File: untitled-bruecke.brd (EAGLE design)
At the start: 100 x 80 mm, 7 parts

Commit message: layout OK
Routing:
- net D6: track 122.9 -> 113.9 mm, vias 2 -> 4
- net D5: track 55.0 -> 49.9 mm
- net B2: track 134.5 -> 131.4 mm
- net C6: track 125.6 -> 128.6 mm, vias 8 -> 6
- net D4: track 113.5 -> 110.5 mm
- net B3: track 124.4 -> 127.4 mm
- net B5: track 171.0 -> 168.1 mm
- net D1: track 46.8 -> 49.6 mm
- net C5: track 133.4 -> 135.2 mm, vias 6 -> 5
- net B1: track 125.5 -> 124.0 mm, vias 4 -> 3
- net B0: track 129.8 -> 128.4 mm
- net C4: track 90.1 -> 89.1 mm
- net D0: track 41.3 -> 40.6 mm
- net C0: vias 5 -> 4

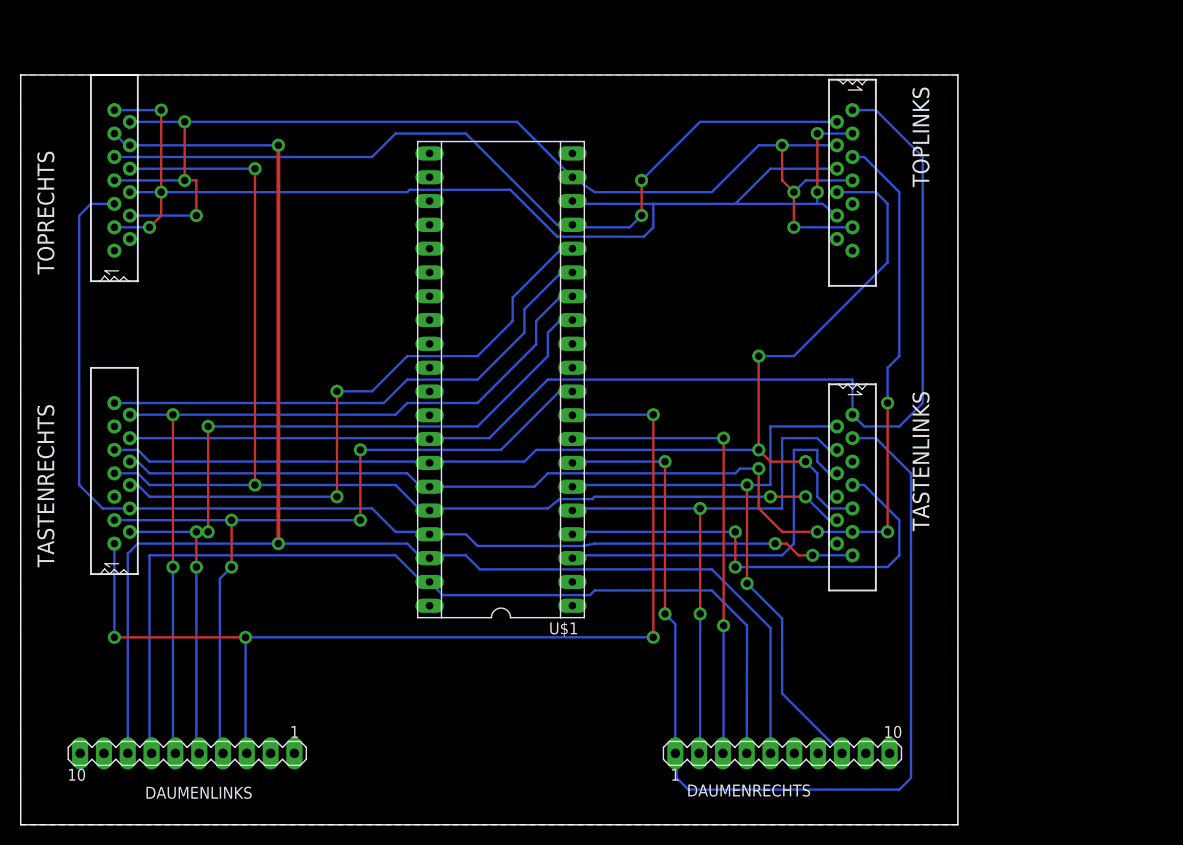
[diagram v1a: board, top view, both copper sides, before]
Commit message: Board für die Fräse vorbereitet
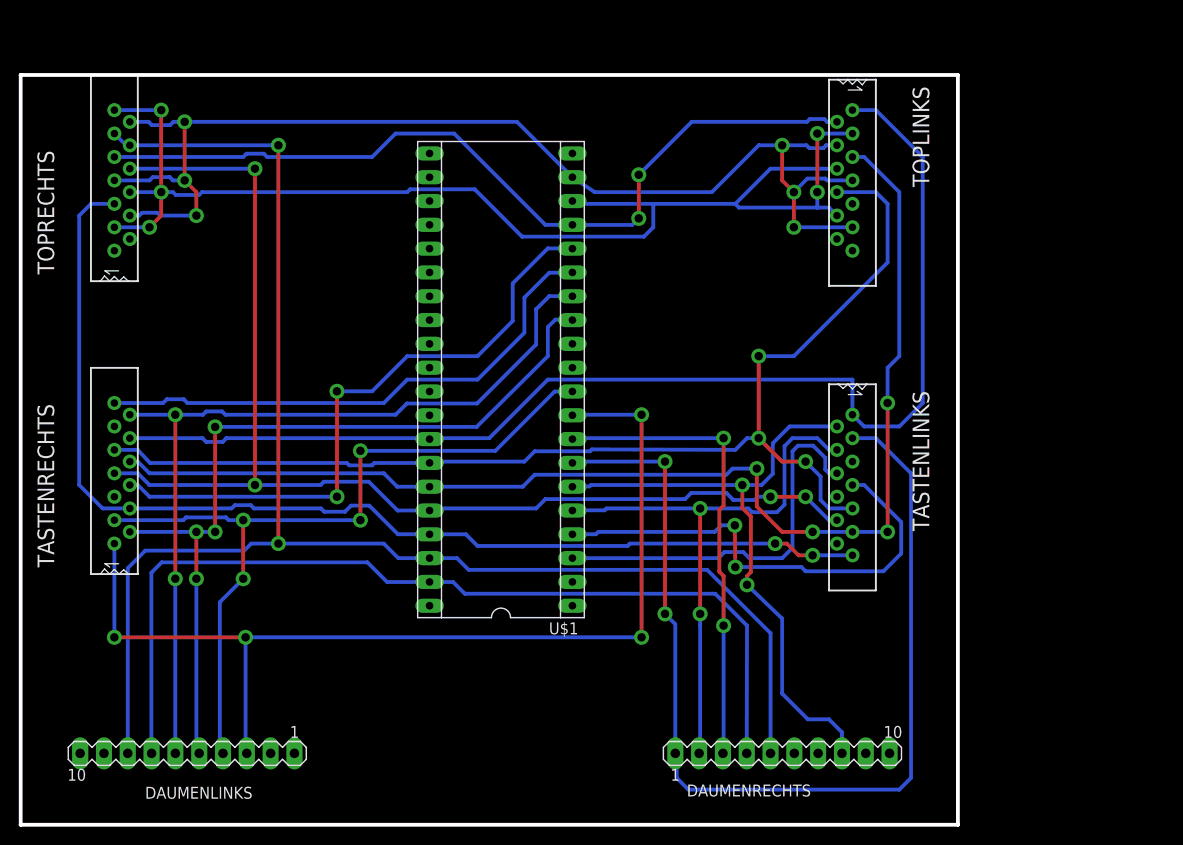
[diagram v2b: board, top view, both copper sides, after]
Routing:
- net D6: track 113.9 -> 111.4 mm
- net B6: track 102.0 -> 99.7 mm
- net D1: track 49.6 -> 51.0 mm
- net B5: track 168.1 -> 166.7 mm
- net D0: track 40.6 -> 41.7 mm
- net C2: track 56.1 -> 57.2 mm
- net B3: track 127.4 -> 128.3 mm
- net C1: track 90.2 -> 91.1 mm
- net B4: track 118.8 -> 119.7 mm
- net C3: track 66.8 -> 67.7 mm
- net C4: track 89.1 -> 90.0 mm
- net C5: track 135.2 -> 135.9 mm
- net D7: track 84.5 -> 85.2 mm
- net D5: track 49.9 -> 50.6 mm
- net C6: track 128.6 -> 129.1 mm

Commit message: Layout fertiggestellt fürs PCB
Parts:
- removed U$1: C-TEENSY++, teensypp:TEENSY++
- added E$1: (no value), holes:3,2-PAD
- added LED1, LED2, LED3, LED4: (no value), led:LED3MM
- added R1, R2, R3, R4: (no value), rcl:R1206
- added U1: C-TEENSY++, teensypp:TEENSY++
- moved TASTENRECHTS 99.2 mm to (108.5, 25.5), flipped to the bottom
- moved TOPRECHTS 95.1 mm to (105.0, 73.5), flipped to the bottom
- moved DAUMENLINKS 81.7 mm to (99.5, 7.00), flipped to the bottom
- moved TASTENLINKS 75.5 mm to (14.0, 25.5), flipped to the bottom
- moved TOPLINKS 71.9 mm to (17.0, 73.5), flipped to the bottom
- moved DAUMENRECHTS 58.8 mm to (22.5, 7.00), flipped to the bottom
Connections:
- removed net VCC: U$1.+5V
- new net N$10: R4.2, U1.F0
- new net N$11: LED1.A, LED2.A, LED3.A, LED4.A, U1.+5V
- new net N$14: LED4.K, R4.1
- new net N$15: LED3.K, R3.1
- new net N$16: LED2.K, R2.1
- new net N$17: LED1.K, R1.1
- new net N$7: R1.2, U1.F3
- new net N$8: R2.2, U1.F2
- new net N$9: R3.2, U1.F1
- net B0: now also U1.B0; no longer U$1.B0
- net B1: now also U1.B1; no longer U$1.B1
- net B2: now also U1.B2; no longer U$1.B2
- net B3: now also TASTENLINKS.P$12, U1.B3; no longer TASTENLINKS.P$10, U$1.B3
- net B4: now also U1.B4; no longer U$1.B4
- net B5: now also U1.B5; no longer U$1.B5
- net B6: now also U1.B6; no longer U$1.B6
- net C0: now also U1.C0; no longer U$1.C0
- net C1: now also U1.C1; no longer U$1.C1
- net C2: now also U1.C2; no longer U$1.C2
- net C3: now also U1.C3; no longer U$1.C3
- net C4: now also U1.C4; no longer U$1.C4
- net C5: now also U1.C5; no longer U$1.C5
- net C6: now also U1.C6; no longer U$1.C6
- net D0: now also TASTENLINKS.P$8, U1.D0; no longer TASTENLINKS.P$6, U$1.D0
- net D1: now also U1.D1; no longer U$1.D1
- net D2: now also TASTENLINKS.P$6, U1.D2; no longer TASTENLINKS.P$4, U$1.D2
- net D3: now also TASTENLINKS.P$4, U1.D3; no longer TASTENLINKS.P$2, U$1.D3
- net D4: now also U1.D4; no longer U$1.D4
- net D5: now also TASTENLINKS.P$2, U1.D5; no longer U$1.D5
- net D6: now also U1.D6; no longer U$1.D6
- net D7: now also U1.D7; no longer U$1.D7
- net GND: now also U1.GRND1; no longer U$1.GRND1
- net N$1: now also U1.GND; no longer U$1.GND
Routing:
- net N$11: track 0.00 -> 72.8 mm
- net D5: track 50.6 -> 122.0 mm, vias 2 -> 0
- net D7: track 85.2 -> 143.6 mm, vias 4 -> 0
- net B4: track 119.7 -> 172.5 mm, vias 2 -> 1
- net D2: track 62.1 -> 109.6 mm, vias 2 -> 0
- net D0: track 41.7 -> 85.3 mm
- net N$10: track 0.00 -> 42.7 mm
- net C0: track 88.7 -> 128.0 mm, vias 4 -> 1
- net B1: track 124.1 -> 162.9 mm, vias 3 -> 1
- net B3: track 128.3 -> 166.9 mm, vias 4 -> 1
- net B2: track 131.2 -> 167.9 mm, vias 4 -> 1
- net N$9: track 0.00 -> 36.0 mm
- net D3: track 67.5 -> 102.2 mm, vias 2 -> 0
- net D6: track 111.4 -> 144.6 mm, vias 4 -> 0
- net D1: track 51.0 -> 83.3 mm, vias 2 -> 0
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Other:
- board size 100 x 80 mm -> 122 x 86 mm
- board text added: "28.02.2013"
- board text added: "CAPS"
- board text added: "KEYPAD"
- board text added: "M. Stapelberg / V. Wunsch"
- board text added: "NUM"
- board text added: "SCR"
- board text added: "Teensy++ Kinesis controller"

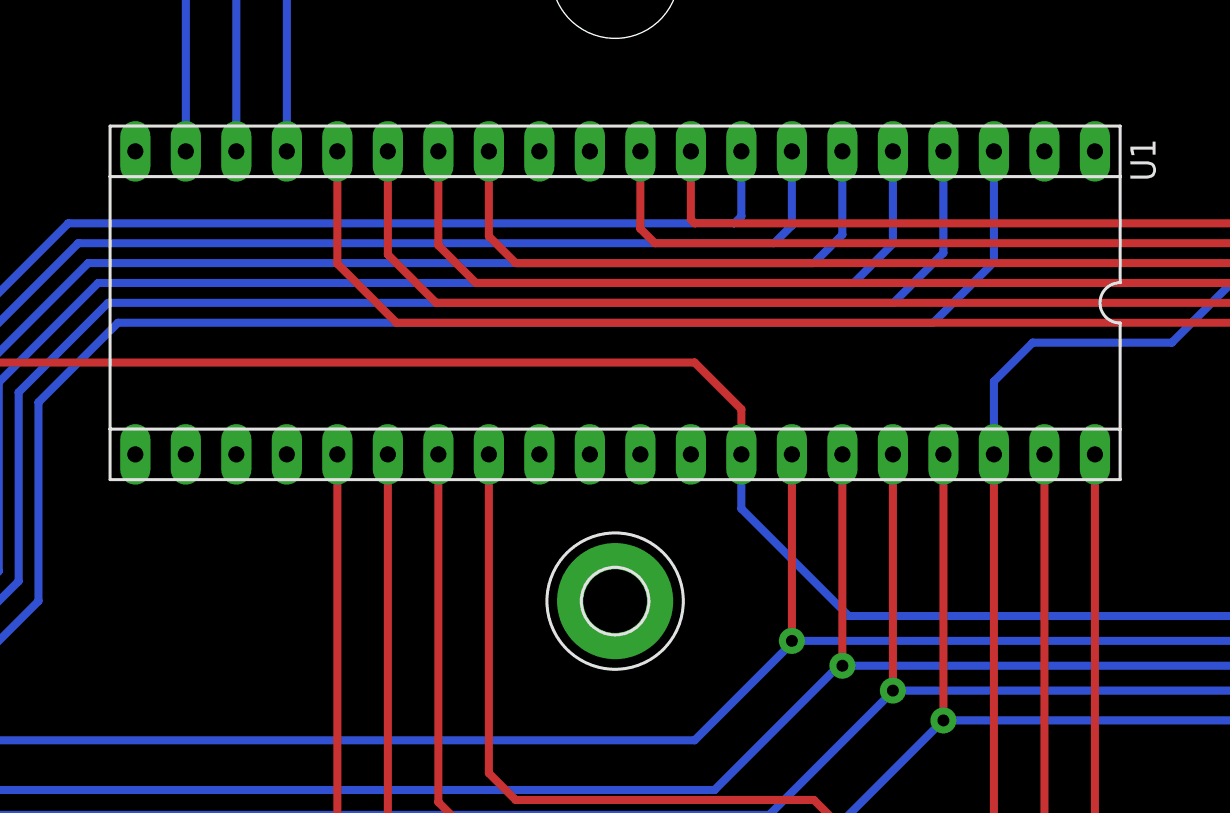
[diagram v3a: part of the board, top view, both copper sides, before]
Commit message: 2013-03-18: Löcher auf richtige Größe gebracht
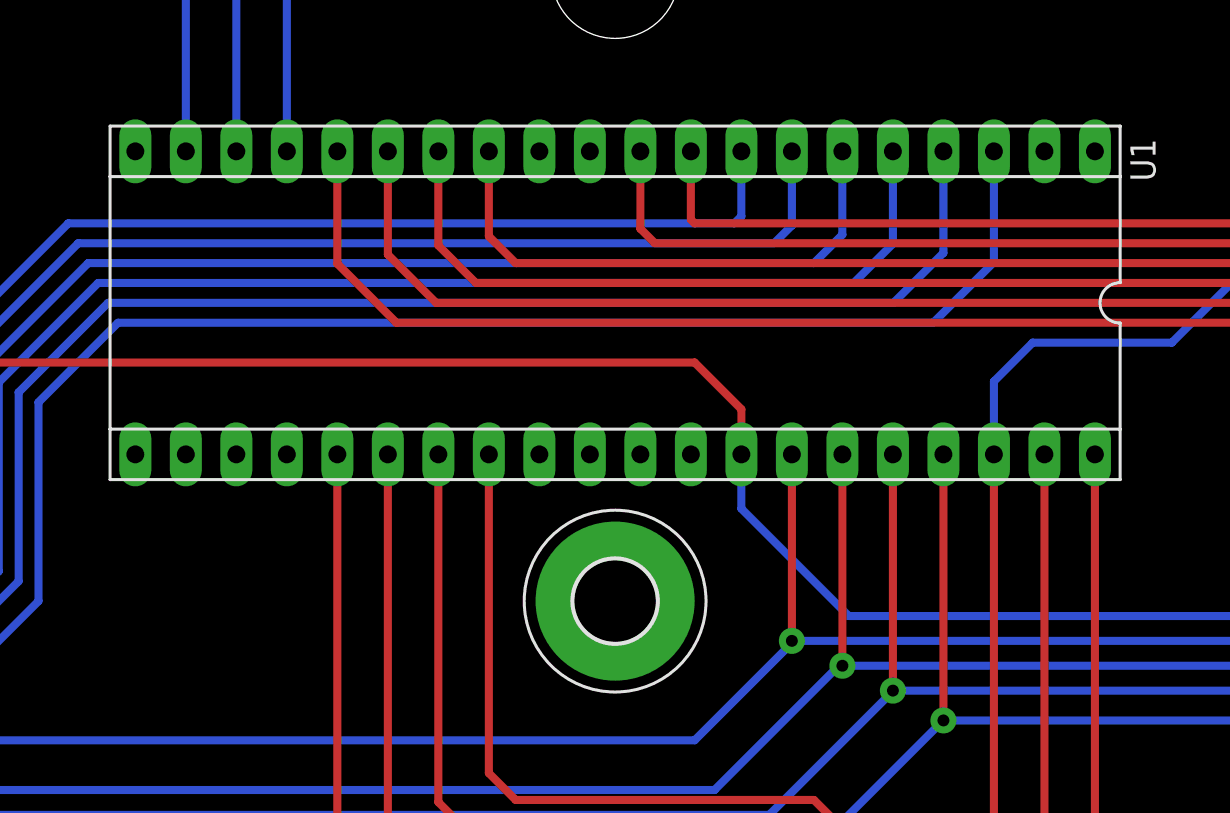
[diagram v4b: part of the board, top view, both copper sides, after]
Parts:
- removed E$1: (no value), holes:3,2-PAD
- added H1: MOUNT-PAD-ROUND4.1, holes:4,1-PAD
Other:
- board text added: "18.03.2013"
- board text removed: "28.02.2013"
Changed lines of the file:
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@@
 <?xml version="1.0" encoding="utf-8"?>
 <!DOCTYPE eagle SYSTEM "eagle.dtd">
-<eagle version="6.2">
+<eagle version="6.3">
 <drawing>
 <settings>
@@
 <grid distance="1" unitdist="mm" unit="mm" style="lines" multiple="1" display="yes" altdistance="0.5" altunitdist="mm" altunit="mm"/>
 <layers>
-<layer number="1" name="Top" color="4" fill="1" visible="yes" active="yes"/>
+<layer number="1" name="Top" color="4" fill="1" visible="no" active="yes"/>
 <layer number="2" name="Route2" color="1" fill="3" visible="yes" active="yes"/>
 <layer number="3" name="Route3" color="4" fill="3" visible="yes" active="yes"/>
@@
 <layer number="14" name="Route14" color="1" fill="6" visible="yes" active="yes"/>
 <layer number="15" name="Route15" color="4" fill="6" visible="yes" active="yes"/>
-<layer number="16" name="Bottom" color="1" fill="1" visible="yes" active="yes"/>
+<layer number="16" name="Bottom" color="1" fill="1" visible="no" active="yes"/>
 <layer number="17" name="Pads" color="2" fill="1" visible="yes" active="yes"/>
 <layer number="18" name="Vias" color="2" fill="1" visible="yes" active="yes"/>
@@
 <circle x="61" y="61.5" radius="5" width="0" layer="41"/>
 <text x="80" y="77" size="2.54" layer="26" rot="MR0">Teensy++ Kinesis controller</text>
-<text x="44" y="62" size="1.778" layer="26" rot="MR0">28.02.2013</text>
+<text x="44" y="62" size="1.778" layer="26" rot="MR0">18.03.2013</text>
 <text x="52" y="58" size="1.778" layer="26" rot="MR0">M. Stapelberg / V. Wunsch</text>
 </plain>
@@
 </class>
 </classes>
-<designrules>
+<designrules name="default">
 <description language="de">&lt;b&gt;EAGLE Design Rules&lt;/b&gt;
 &lt;p&gt;
@@
 <attribute name="VALUE" x="10.19" y="35.66" size="1.778" layer="28" rot="MR270"/>
 </element>
-<element name="E$1" library="holes" package="3,2-PAD" value="" x="61" y="30" smashed="yes"/>
 <element name="LED1" library="led" package="LED3MM" value="" x="45.75" y="3.5" smashed="yes" rot="R90">
 <attribute name="NAME" x="50.369" y="1.405" size="1.27" layer="25" ratio="10" rot="R90"/>
@@
 <attribute name="VALUE" x="78.663" y="9.603" size="1.27" layer="27" rot="R90"/>
 </element>
+<element name="H1" library="holes" package="4,1-PAD" value="MOUNT-PAD-ROUND4.1" x="61" y="30"/>
 </elements>
 <signals>
 <signal name="GND">
-<contactref element="U1" pad="GRND1"/>
 <polygon width="0.4064" layer="1">
 <vertex x="1" y="85"/>
@@
 <vertex x="121" y="85"/>
 </polygon>
+<contactref element="U1" pad="GRND1"/>
+<wire x1="120" y1="73" x2="120" y2="84" width="0" layer="19" extent="1-1"/>
+<wire x1="108" y1="84" x2="120" y2="84" width="0" layer="19" extent="1-1"/>
+<wire x1="120" y1="61" x2="120" y2="73" width="0" layer="19" extent="1-1"/>
+<wire x1="96" y1="84" x2="108" y2="84" width="0" layer="19" extent="1-1"/>
+<wire x1="96" y1="74" x2="96" y2="84" width="0" layer="19" extent="1-1"/>
+<wire x1="96" y1="71" x2="96" y2="74" width="0" layer="19" extent="1-1"/>
+<wire x1="84" y1="84" x2="96" y2="84" width="0" layer="19" extent="1-1"/>
+<wire x1="73" y1="84" x2="84" y2="84" width="0" layer="19" extent="1-1"/>
+<wire x1="120" y1="49" x2="120" y2="61" width="0" layer="19" extent="1-1"/>
+<wire x1="120" y1="38" x2="120" y2="49" width="0" layer="19" extent="1-1"/>
+<wire x1="113" y1="36" x2="120" y2="38" width="0" layer="19" extent="1-1"/>
+<wire x1="61" y1="84" x2="73" y2="84" width="0" layer="19" extent="1-1"/>
+<wire x1="120" y1="26" x2="120" y2="38" width="0" layer="19" extent="1-1"/>
+<wire x1="49" y1="84" x2="61" y2="84" width="0" layer="19" extent="1-1"/>
+<wire x1="38" y1="84" x2="49" y2="84" width="0" layer="19" extent="1-1"/>
+<wire x1="120" y1="14" x2="120" y2="26" width="0" layer="19" extent="1-1"/>
+<wire x1="113" y1="11" x2="120" y2="14" width="0" layer="19" extent="1-1"/>
+<wire x1="120" y1="2" x2="113" y2="11" width="0" layer="19" extent="1-1"/>
+<wire x1="26" y1="84" x2="38" y2="84" width="0" layer="19" extent="1-1"/>
+<wire x1="22" y1="76" x2="26" y2="84" width="0" layer="19" extent="1-1"/>
+<wire x1="22" y1="71" x2="22" y2="76" width="0" layer="19" extent="1-1"/>
+<wire x1="14" y1="84" x2="22" y2="76" width="0" layer="19" extent="1-1"/>
+<wire x1="2" y1="84" x2="14" y2="84" width="0" layer="19" extent="1-1"/>
+<wire x1="2" y1="73" x2="2" y2="84" width="0" layer="19" extent="1-1"/>
+<wire x1="2" y1="61" x2="2" y2="73" width="0" layer="19" extent="1-1"/>
+<wire x1="2" y1="49" x2="2" y2="61" width="0" layer="19" extent="1-1"/>
+<wire x1="2" y1="38" x2="2" y2="49" width="0" layer="19" extent="1-1"/>
+<wire x1="2" y1="26" x2="2" y2="38" width="0" layer="19" extent="1-1"/>
+<wire x1="2" y1="14" x2="2" y2="26" width="0" layer="19" extent="1-1"/>
+<wire x1="2" y1="2" x2="2" y2="14" width="0" layer="19" extent="1-1"/>
+<wire x1="13" y1="2" x2="2" y2="2" width="0" layer="19" extent="1-1"/>
+<wire x1="24" y1="2" x2="13" y2="2" width="0" layer="19" extent="1-1"/>
+<wire x1="35" y1="2" x2="24" y2="2" width="0" layer="19" extent="1-1"/>
+<wire x1="41" y1="6" x2="35" y2="2" width="0" layer="19" extent="1-1"/>
+<wire x1="51" y1="6" x2="41" y2="6" width="0" layer="19" extent="1-1"/>
+<wire x1="61" y1="6" x2="51" y2="6" width="0" layer="19" extent="1-1"/>
+<wire x1="71" y1="6" x2="61" y2="6" width="0" layer="19" extent="1-1"/>
+<wire x1="81" y1="6" x2="71" y2="6" width="0" layer="19" extent="1-1"/>
+<wire x1="84" y1="2" x2="81" y2="6" width="0" layer="19" extent="1-1"/>
+<wire x1="93" y1="2" x2="84" y2="2" width="0" layer="19" extent="1-1"/>
+<wire x1="59.73" y1="37.38" x2="61" y2="6" width="0" layer="19" extent="1-1"/>
 </signal>
 <signal name="N$12">
